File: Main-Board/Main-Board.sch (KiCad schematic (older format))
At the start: 0 parts

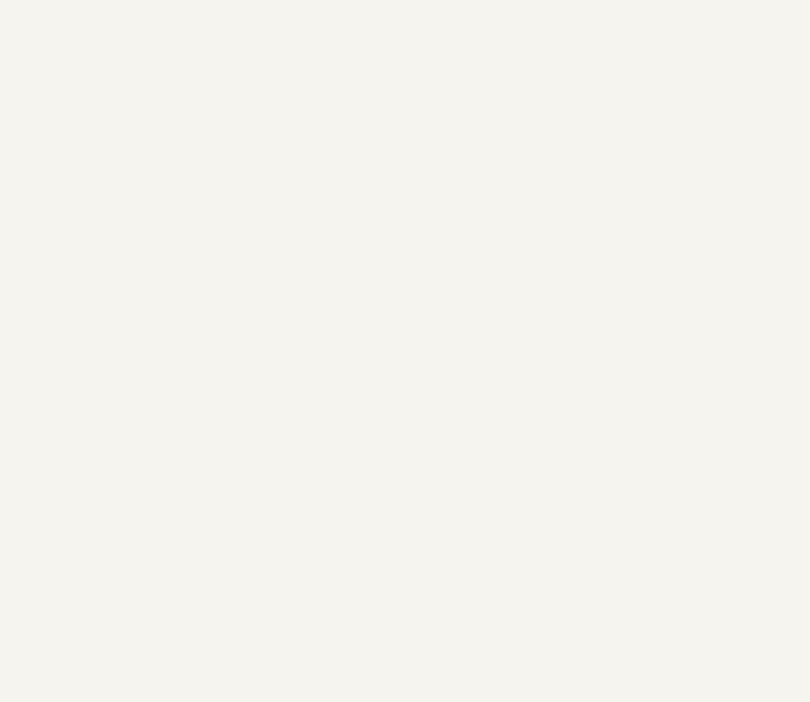
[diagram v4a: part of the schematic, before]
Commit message: Roughed the rest of the microcontroller schematic
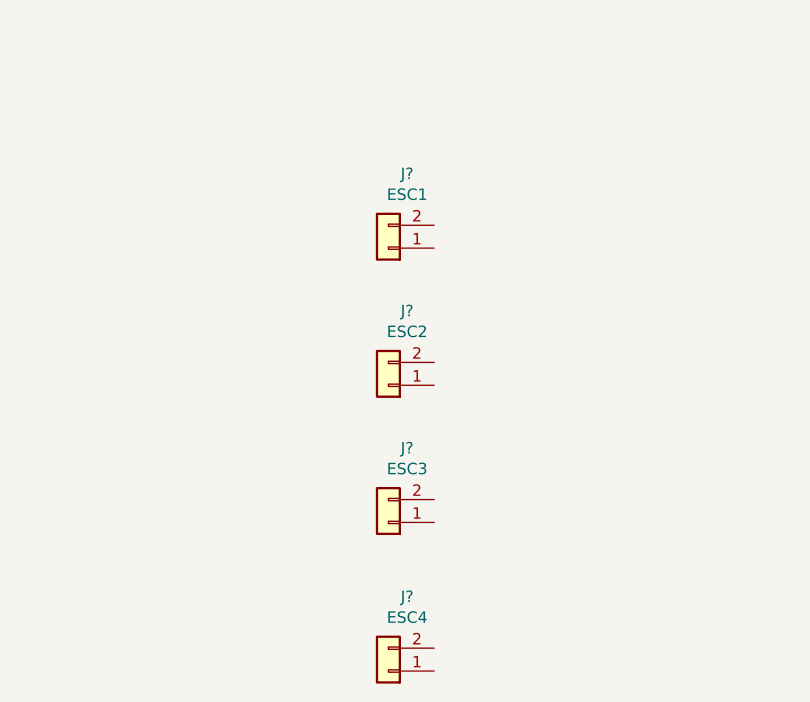
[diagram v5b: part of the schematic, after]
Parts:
- added J?: ESC1, symbol Connector_Generic:Conn_01x02
- added J?: ESC2, symbol Connector_Generic:Conn_01x02
- added J?: ESC3, symbol Connector_Generic:Conn_01x02
- added J?: ESC4, symbol Connector_Generic:Conn_01x02
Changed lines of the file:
@@
 Text Notes 8250 4850 0    50   ~ 0
 Debug port? Extra spare PWM?\n
+$Comp
+L Connector_Generic:Conn_01x02 J?
+U 1 1 60055D25
+P 4650 3150
+F 0 "J?" H 4568 2825 50  0000 C CNN
+F 1 "ESC1" H 4568 2916 50  0000 C CNN
+F 2 "" H 4650 3150 50  0001 C CNN
+F 3 "~" H 4650 3150 50  0001 C CNN
+	1    4650 3150
+	-1   0    0    1
+$EndComp
+$Comp
+L Connector_Generic:Conn_01x02 J?
+U 1 1 60056CDE
+P 4650 3750
+F 0 "J?" H 4568 3425 50  0000 C CNN
+F 1 "ESC2" H 4568 3516 50  0000 C CNN
+F 2 "" H 4650 3750 50  0001 C CNN
+F 3 "~" H 4650 3750 50  0001 C CNN
+	1    4650 3750
+	-1   0    0    1
+$EndComp
+$Comp
+L Connector_Generic:Conn_01x02 J?
+U 1 1 60056F29
+P 4650 4350
+F 0 "J?" H 4568 4025 50  0000 C CNN
+F 1 "ESC3" H 4568 4116 50  0000 C CNN
+F 2 "" H 4650 4350 50  0001 C CNN
+F 3 "~" H 4650 4350 50  0001 C CNN
+	1    4650 4350
+	-1   0    0    1
+$EndComp
+$Comp
+L Connector_Generic:Conn_01x02 J?
+U 1 1 600574C6
+P 4650 5000
+F 0 "J?" H 4568 4675 50  0000 C CNN
+F 1 "ESC4" H 4568 4766 50  0000 C CNN
+F 2 "" H 4650 5000 50  0001 C CNN
+F 3 "~" H 4650 5000 50  0001 C CNN
+	1    4650 5000
+	-1   0    0    1
+$EndComp
 $EndSCHEMATC

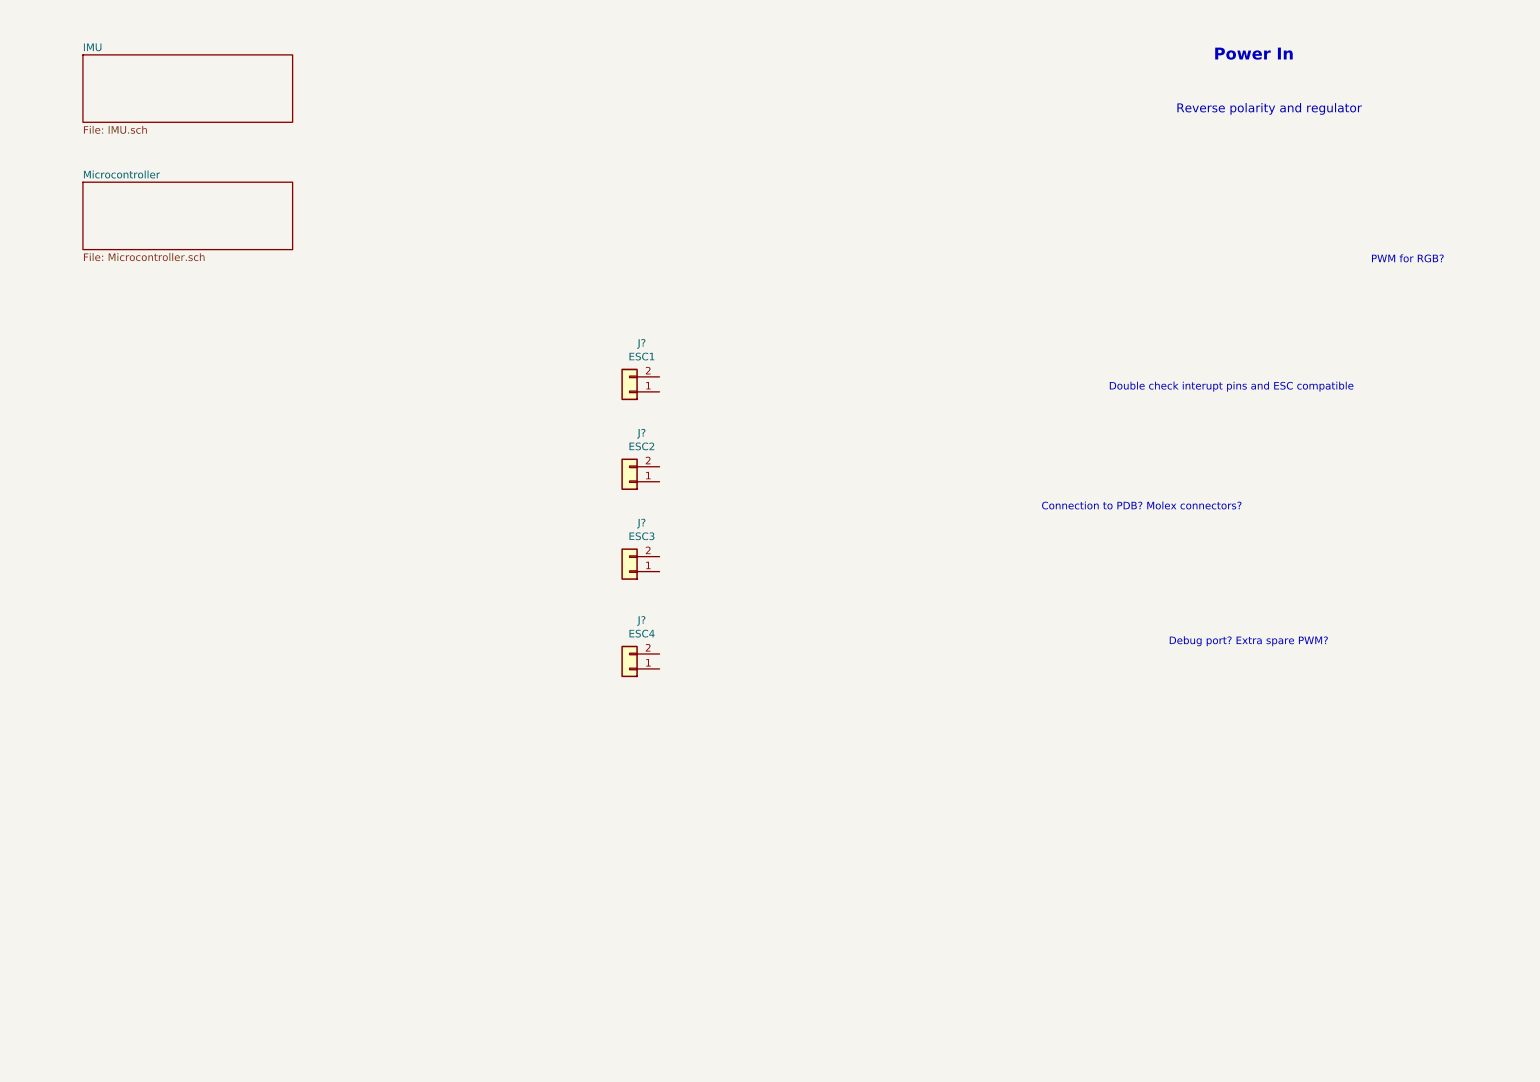
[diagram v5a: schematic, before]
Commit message: Added battery monitoring, some RGB LED, and general org
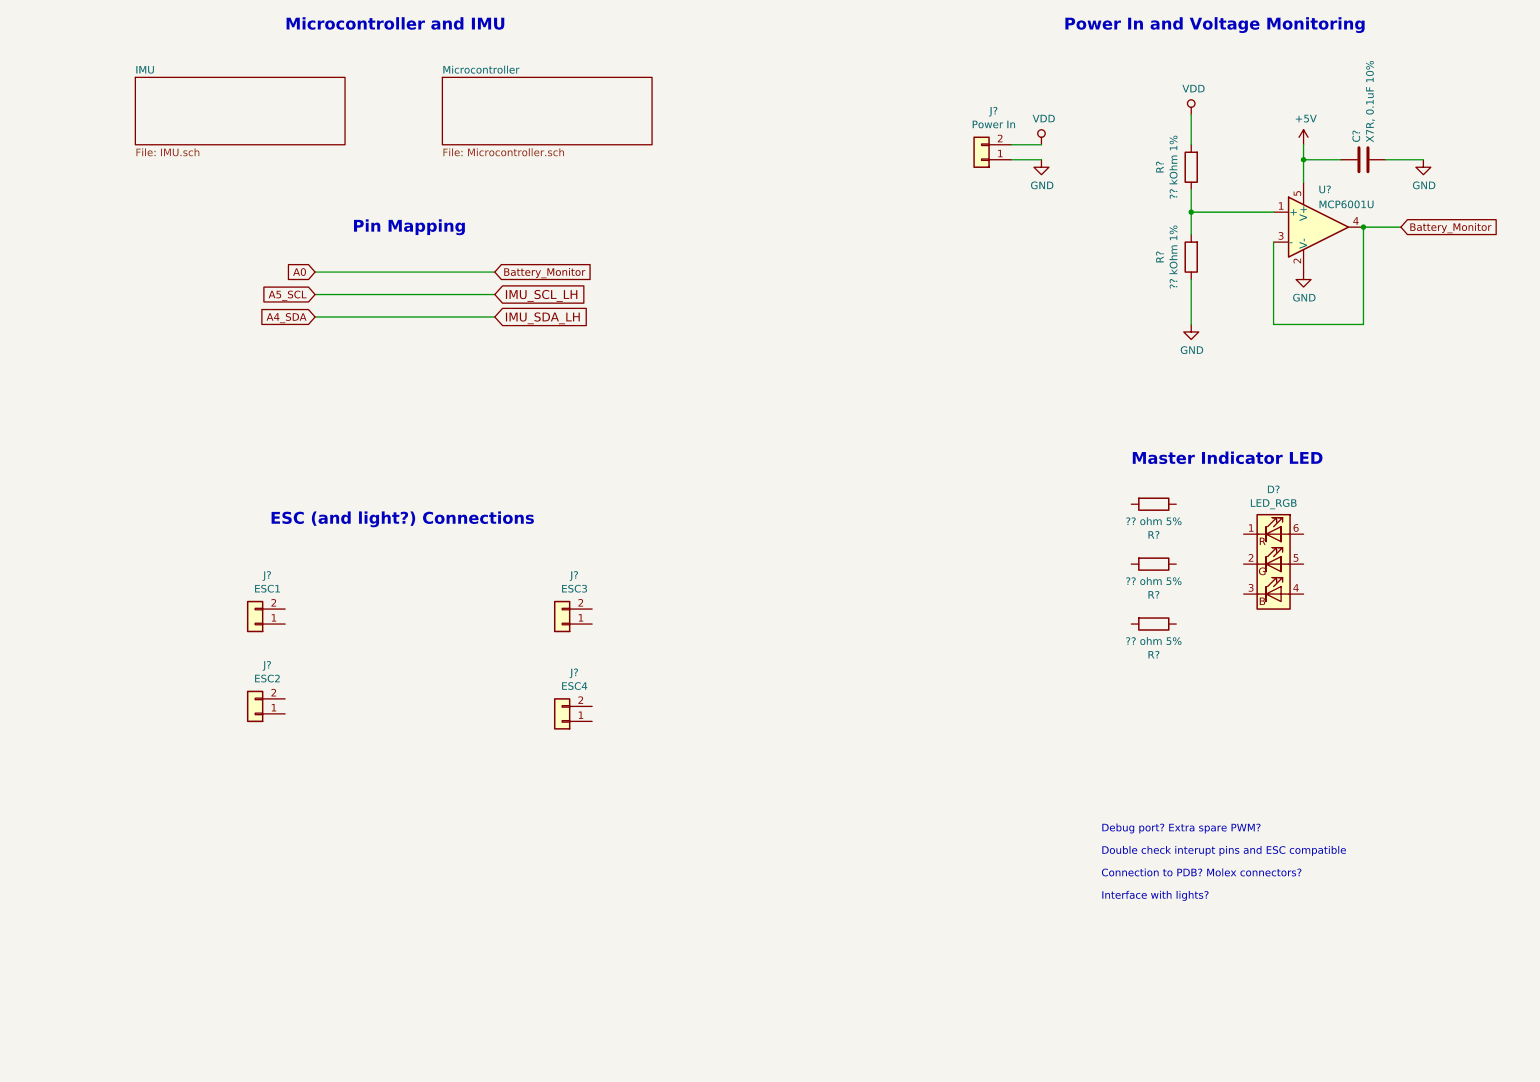
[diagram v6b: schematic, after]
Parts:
- added C?: X7R, 0.1uF 10%, Capacitor_SMD:C_0603_1608Metric_Pad1.05x0.95mm_HandSolder, symbol Device:C
- added D?: LED_RGB, symbol Device:LED_RGB
- added J?: Power In, symbol Connector_Generic:Conn_01x02
- added R? (x2): ?? kOhm 1%, Resistor_SMD:R_0603_1608Metric_Pad1.05x0.95mm_HandSolder, symbol Device:R
- added R? (x3): ?? ohm 5%, Resistor_SMD:R_0603_1608Metric_Pad1.05x0.95mm_HandSolder, symbol Device:R
- added U?: MCP6001U, symbol Amplifier_Operational:MCP6001U
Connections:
- new net: R?.1, R?.2, U?.1 (+)
- new net +5V: C?.1, U?.5 (V+)
- new net A0: U?.3 (-), U?.4
- new net GND: C?.2, J?.1 (Pin_1), R?.1, U?.2 (V-)
- new net VDD: J?.2 (Pin_2), R?.2
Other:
- note added: "ESC (and light?) Connections"
- note added: "Interface with lights?"
- note added: "Master Indicator LED"
- note added: "Microcontroller and IMU"
- note added: "Pin Mapping"
- note added: "Power In and Voltage Monitoring"
- note removed: "PWM for RGB?"
- note removed: "Power In"
- note removed: "Reverse polarity and regulator"
- moved on the sheet: J?

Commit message: Add RGB LED and added some additional pinout
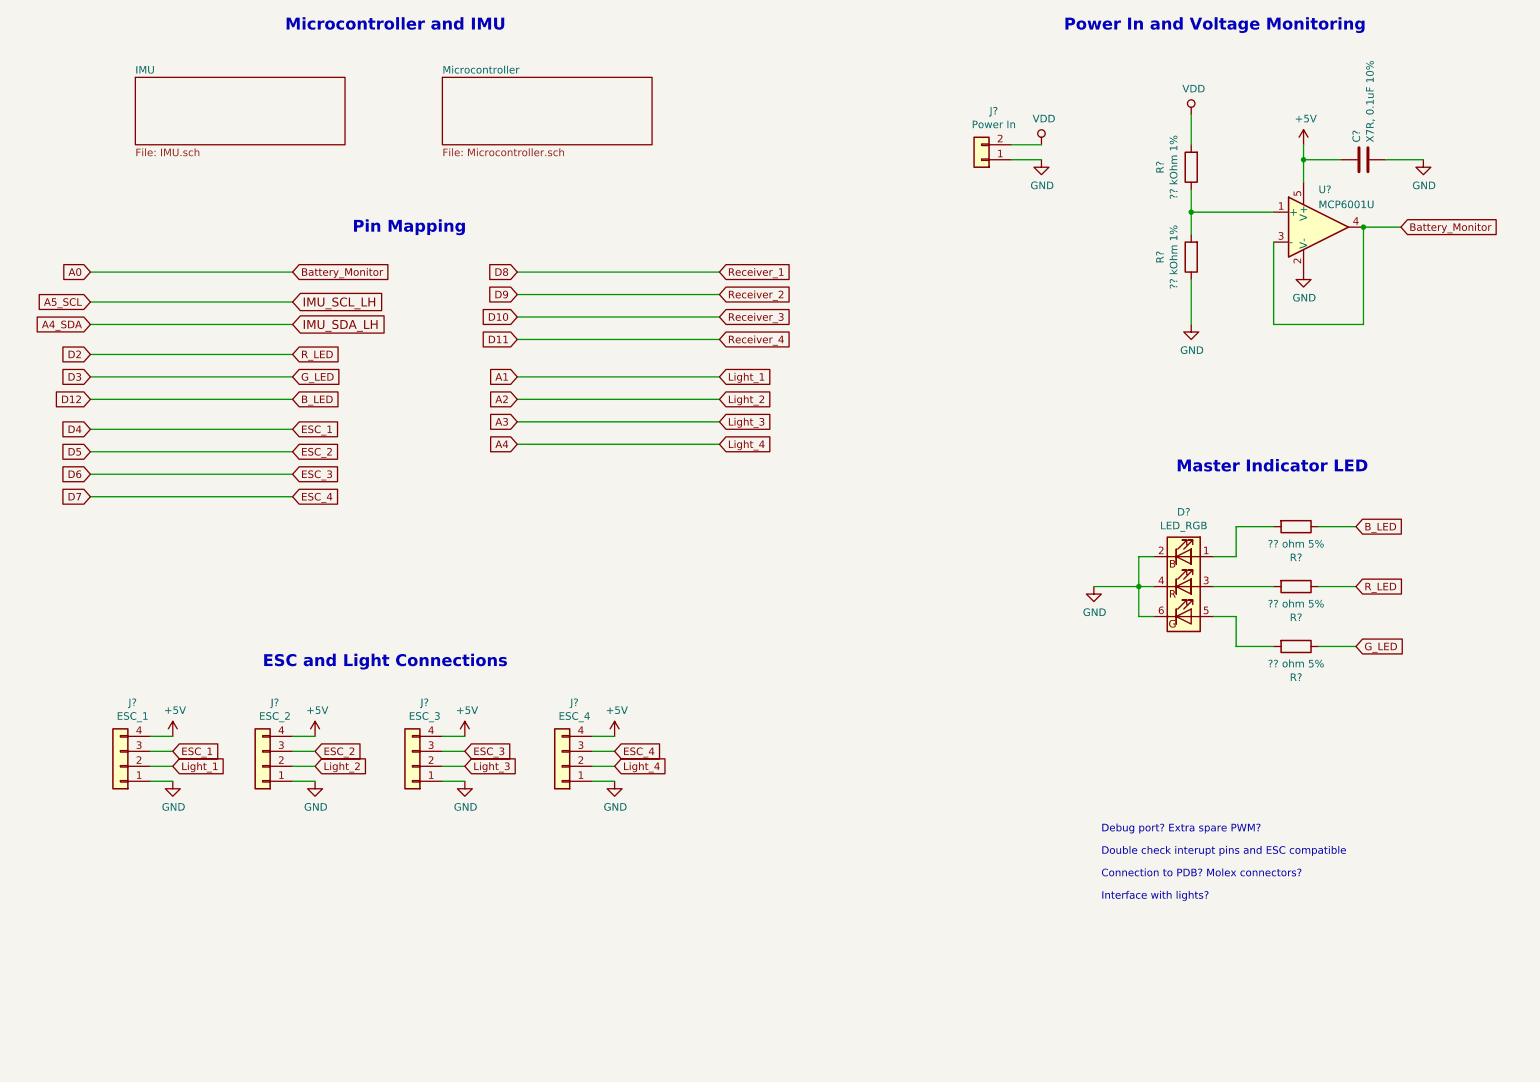
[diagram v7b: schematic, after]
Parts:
- removed D?: LED_RGB, symbol Device:LED_RGB
- removed J?: ESC1, symbol Connector_Generic:Conn_01x02
- removed J?: ESC2, symbol Connector_Generic:Conn_01x02
- removed J?: ESC3, symbol Connector_Generic:Conn_01x02
- removed J?: ESC4, symbol Connector_Generic:Conn_01x02
- added D?: LED_RGB, symbol Custom:LED_RGB
- added J?: ESC_1, Connector_PinHeader_2.54mm:PinHeader_1x04_P2.54mm_Vertical, symbol Connector_Generic:Conn_01x04
- added J?: ESC_2, Connector_PinHeader_2.54mm:PinHeader_1x04_P2.54mm_Vertical, symbol Connector_Generic:Conn_01x04
- added J?: ESC_3, Connector_PinHeader_2.54mm:PinHeader_1x04_P2.54mm_Vertical, symbol Connector_Generic:Conn_01x04
- added J?: ESC_4, Connector_PinHeader_2.54mm:PinHeader_1x04_P2.54mm_Vertical, symbol Connector_Generic:Conn_01x04
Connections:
- net +5V: now also J?.4 (Pin_4), J?.4 (Pin_4), J?.4 (Pin_4), J?.4 (Pin_4)
- net GND: now also D?.2 (RK), D?.4 (GK), D?.6 (BK), J?.1 (Pin_1), J?.1 (Pin_1), J?.1 (Pin_1), J?.1 (Pin_1)
- net B_LED: now reaches R?.1
- net at R?.2: now also D?.1 (RA)
- net D2: now reaches R?.1
- net at R?.2: now also D?.3 (GA)
- net D3: now reaches R?.1
- net at R?.2: now also D?.5 (BA)
- new net A1: J?.2 (Pin_2)
- new net A2: J?.2 (Pin_2)
- new net A3: J?.2 (Pin_2)
- new net A4: J?.2 (Pin_2)
- new net D4: J?.3 (Pin_3)
- new net D5: J?.3 (Pin_3)
- new net D6: J?.3 (Pin_3)
- new net D7: J?.3 (Pin_3)
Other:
- note added: "ESC and Light Connections"
- note removed: "ESC (and light?) Connections"
- moved on the sheet: R?

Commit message: Added a few more footprints and component specifics. Created first net list
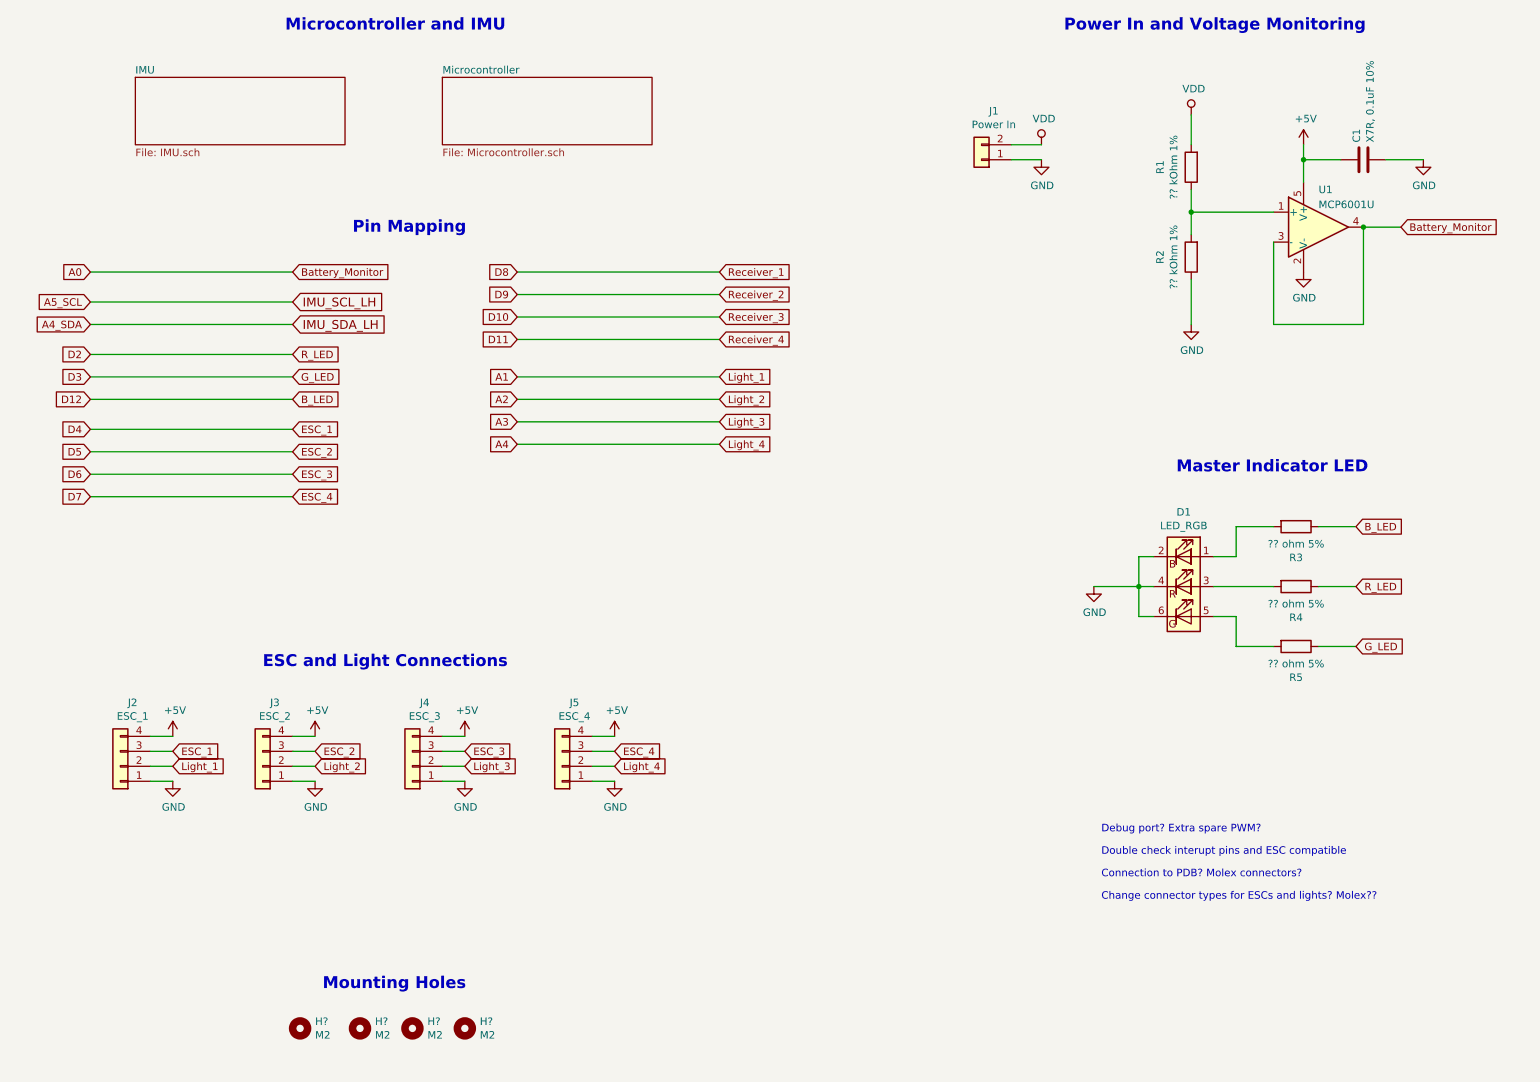
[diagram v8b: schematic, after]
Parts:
- added H? (x4): M2, MountingHole:MountingHole_2.2mm_M2_ISO7380_Pad, symbol Mechanical:MountingHole
- J1: renamed from J?; footprint (none) -> Connector_Molex:Molex_Micro-Fit_3.0_43650-0200_1x02_P3.00mm_Horizontal
- U1: renamed from U?; footprint (none) -> Package_TO_SOT_SMD:SOT-23-5; Digi-Key # (none) -> MCP6001UT-I/OTCT-ND; Manufacturer (none) -> Microchip Technology; Manufacturer # (none) -> MCP6001UT-I/OT
- gave numbers to parts that had none: 11
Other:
- note added: "Change connector types for ESCs and lights? Molex??"
- note added: "Mounting Holes"
- note removed: "Interface with lights?"
